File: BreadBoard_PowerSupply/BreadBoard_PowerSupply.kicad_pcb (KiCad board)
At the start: 2 copper layers, 33 x 58.2 mm, 18 parts, among them J1 Conn_01x02_Pin, J2 Conn_01x02_Pin, J3 Conn_01x03_Pin, J4 Conn_01x03_Pin, J5 Screw_Terminal_01x02, J6 Barrel_Jack_Switch, J7 Screw_Terminal_01x02, U1 LM7805_TO220, U2 LM317_TO-220

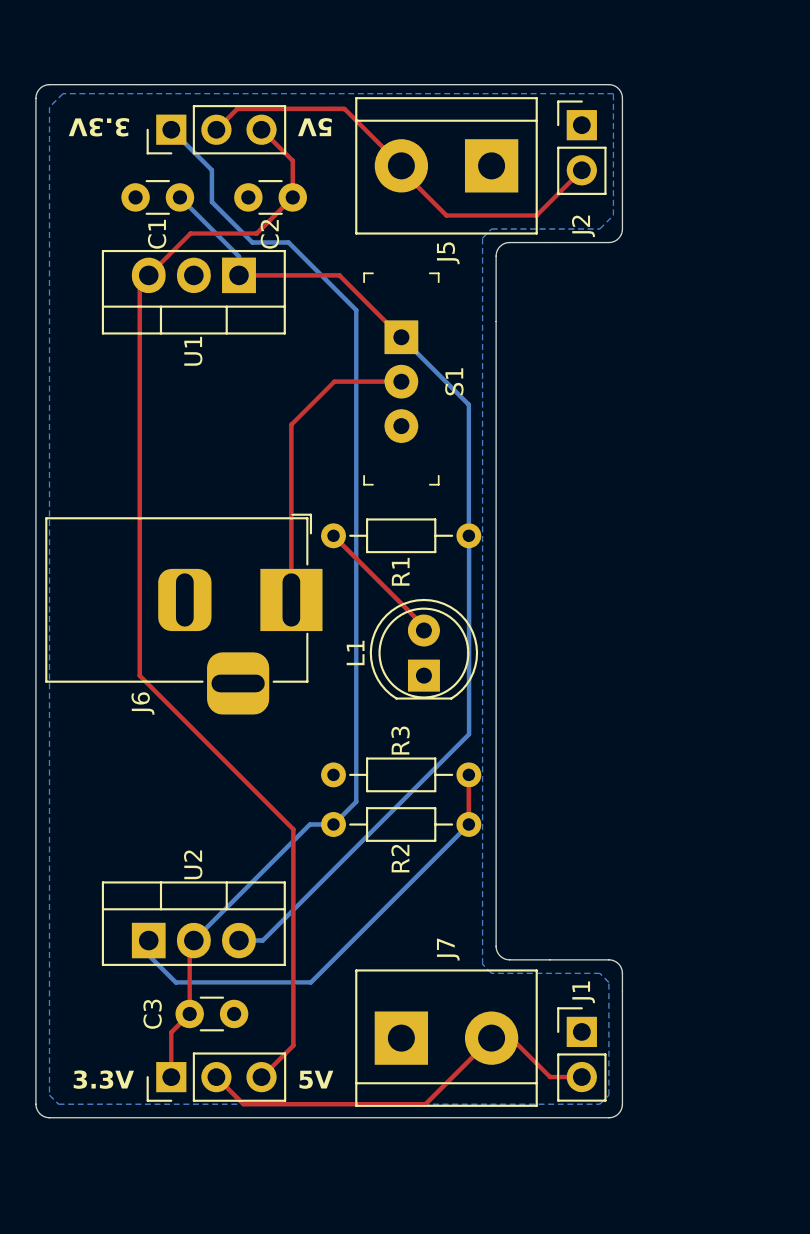
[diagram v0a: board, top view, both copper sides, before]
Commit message: Updated
12V and 9V circuit added to schematics, components arranged on PCB,

Just have to confirm the sizes of components with available components in inventory and make the connections
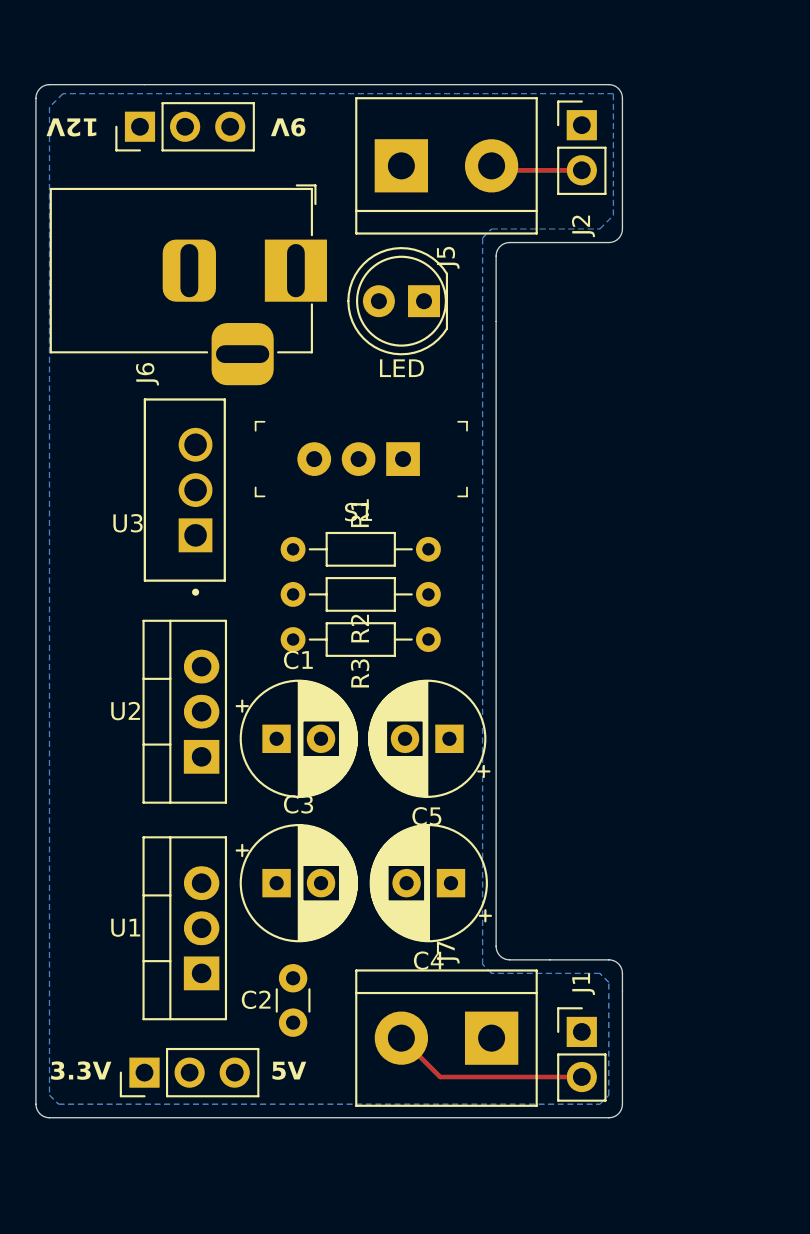
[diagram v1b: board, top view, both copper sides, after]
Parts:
- removed REF**: KiCad-Logo2_5mm_SilkScreen, Symbol:KiCad-Logo2_5mm_SilkScreen
- added C4: 220u, Capacitor_THT:CP_Radial_D6.3mm_P2.50mm, F.Cu at (175.3, 110.7)
- added C5: 47u, Capacitor_THT:CP_Radial_D6.3mm_P2.50mm, F.Cu at (175.2, 102.6)
- added U3: L7809, L7809CV:TO255P1020X450X1968-3B, F.Cu at (160.9, 88.6)
- C1, C3: footprint Capacitor_THT:C_Disc_D3.0mm_W1.6mm_P2.50mm -> Capacitor_THT:CP_Radial_D6.3mm_P2.50mm
- D1: value L1 -> LED
- moved C2 46.5 mm to (166.4, 118.6), turned to 90 degrees
- moved U1 39.4 mm to (161.2, 115.8), turned to 90 degrees
- moved C1 31.0 mm to (165.4, 102.6), turned to 0 degrees
- moved D1 21.1 mm to (173.7, 78.0), turned to 180 degrees
- moved J6 18.5 mm to (166.5, 76.3)
- moved R2 13.2 mm to (174.0, 94.5)
- moved U2 10.8 mm to (161.2, 103.6), turned to 90 degrees
- moved R3 9.31 mm to (174.0, 97.0), turned to 180 degrees
- moved C3 7.75 mm to (165.4, 110.7), turned to 0 degrees
- moved S1 6.86 mm to (172.6, 86.9), turned to 180 degrees
- moved R1 5.40 mm to (174.0, 91.9), turned to 180 degrees
- moved J5 5.08 mm to (172.5, 70.4), turned to 0 degrees
- moved J7 5.08 mm to (177.5, 119.5), turned to 180 degrees
- moved J4 1.77 mm to (157.7, 68.2)
- moved J3 1.53 mm to (158.0, 121.4)
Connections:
- C3 pad 1: GND -> /3.3V
- C3 pad 2: /3.3V -> GND
- J4 pad 1: /3.3V -> /12V
- J4 pad 3: /5V -> /9V
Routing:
- net /5V: track 64.2 -> 0.00 mm
- net /3.3V: track 63.9 -> 0.00 mm
- net /12V: track 58.0 -> 0.00 mm
- net Net-(U2-ADJ): track 26.0 -> 0.00 mm
- net /PWR_OUTPUT_1: track 24.7 -> 5.66 mm
- net /PWR_INPUT: track 17.1 -> 0.00 mm
- net /PWR_OUTPUT_2: track 23.7 -> 11.1 mm
- net Net-(D1-A): track 8.19 -> 0.00 mm
- net GND: track 0.48 -> 1.36 mm
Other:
- board text added: "12V"
- board text added: "9V"

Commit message: updates
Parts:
- moved R2 27.3 mm to (164.1, 119.9), turned to 90 degrees
- moved S1 20.2 mm to (167.9, 106.5), turned to 90 degrees
- moved C5 19.7 mm to (172.8, 83.1), turned to 0 degrees
- moved D1 17.3 mm to (189.2, 85.9), turned to 0 degrees
- moved J4 15.4 mm to (170.2, 77.2)
- moved J3 15.4 mm to (170.7, 112.8)
- moved C1 14.5 mm to (172.8, 90.2)
- moved R1 14.4 mm to (164.1, 81.5), turned to -90 degrees
- moved C4 13.7 mm to (172.8, 97.3), turned to 0 degrees
- moved C2 12.9 mm to (175.2, 109.2), turned to 180 degrees
- moved R3 9.91 mm to (164.1, 96.8), turned to -90 degrees
- moved C3 9.73 mm to (172.8, 104.4)
- moved J6 5.43 mm to (167.1, 70.9)
- moved U3 3.33 mm to (160.4, 85.3)
- moved U1 2.84 mm to (160.7, 118.6)
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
